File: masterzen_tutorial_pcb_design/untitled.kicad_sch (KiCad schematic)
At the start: 192 parts, among them SW1 SW_Push, SW10 SW_Push, SW11 SW_Push, SW12 SW_Push, SW13 SW_Push, SW14 SW_Push, SW15 SW_Push, SW16 SW_Push, SW17 SW_Push, SW18 SW_Push, SW19 SW_Push, SW2 SW_Push, SW20 SW_Push, SW21 SW_Push, SW22 SW_Push, SW23 SW_Push, SW24 SW_Push, SW25 SW_Push, SW26 SW_Push, SW27 SW_Push, SW28 SW_Push, SW29 SW_Push, SW3 SW_Push, SW30 SW_Push, SW31 SW_Push, SW32 SW_Push, SW33 SW_Push, SW34 SW_Push, SW35 SW_Push, SW36 SW_Push, SW37 SW_Push, SW38 SW_Push, SW39 SW_Push, SW4 SW_Push, SW40 SW_Push, SW41 SW_Push, SW42 SW_Push, SW43 SW_Push, SW44 SW_Push, SW45 SW_Push, SW46 SW_Push, SW47 SW_Push, SW48 SW_Push, SW49 SW_Push, SW5 SW_Push, SW50 SW_Push, SW51 SW_Push, SW52 SW_Push, SW53 SW_Push, SW54 SW_Push, SW55 SW_Push, SW56 SW_Push, SW57 SW_Push, SW58 SW_Push, SW59 SW_Push, SW6 SW_Push, SW60 SW_Push, SW61 SW_Push, SW62 SW_Push, SW63 SW_Push, SW64 SW_Push, SW65 SW_Push, SW66 SW_Push, SW67 SW_Push, SW68 SW_Push, SW69 SW_Push, SW7 SW_Push, SW70 SW_Push, SW71 SW_Push, SW72 SW_Push, SW73 SW_Push, SW74 SW_Push, SW75 SW_Push, SW76 SW_Push, SW77 SW_Push, SW78 SW_Push, SW79 SW_Push, SW8 SW_Push, SW80 SW_Push, SW81 SW_Push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

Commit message: Updated Schematic with correct keys
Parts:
- removed D31, D47, D62, D63, D76, D78, D84, D85, D87, D88, D89, D92: D, symbol Device:D
- removed SW31, SW47, SW62, SW63, SW76, SW78, SW84, SW85, SW87, SW88, SW89, SW92: SW_Push, symbol Switch:SW_Push
- renumbered D32 to D31, D33 to D32, D34 to D33, D35 to D34, D36 to D35, D37 to D36, D38 to D37, D39 to D38, D40 to D39, D41 to D40, D42 to D41, D43 to D42, D44 to D43, D45 to D44, D46 to D45, D48 to D46, D49 to D47, D50 to D48, D51 to D49, D52 to D50, D53 to D51, D54 to D52, D55 to D53, D56 to D54, D57 to D55, D58 to D56, D59 to D57, D60 to D58, D61 to D59, D64 to D60, D65 to D61, D66 to D62, D67 to D63, D68 to D64, D69 to D65, D70 to D66, D71 to D67, D72 to D68, D73 to D69, D74 to D70, D75 to D71, D77 to D72, D79 to D73, D80 to D74, D81 to D75, D82 to D76, D83 to D77, D86 to D78, D90 to D79, D91 to D80, D93 to D81, D94 to D82, D95 to D83, D96 to D84, SW32 to SW31, SW33 to SW32, SW34 to SW33, SW35 to SW34, SW36 to SW35, SW37 to SW36, SW38 to SW37, SW39 to SW38, SW40 to SW39, SW41 to SW40, SW42 to SW41, SW43 to SW42, SW44 to SW43, SW45 to SW44, SW46 to SW45, SW48 to SW46, SW49 to SW47, SW50 to SW48, SW51 to SW49, SW52 to SW50, SW53 to SW51, SW54 to SW52, SW55 to SW53, SW56 to SW54, SW57 to SW55, SW58 to SW56, SW59 to SW57, SW60 to SW58, SW61 to SW59, SW64 to SW60, SW65 to SW61, SW66 to SW62, SW67 to SW63, SW68 to SW64, SW69 to SW65, SW70 to SW66, SW71 to SW67, SW72 to SW68, SW73 to SW69, SW74 to SW70, SW75 to SW71, SW77 to SW72, SW79 to SW73, SW80 to SW74, SW81 to SW75, SW82 to SW76, SW83 to SW77, SW86 to SW78, SW90 to SW79, SW91 to SW80, SW93 to SW81, SW94 to SW82, SW95 to SW83, SW96 to SW84
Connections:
- net col15: now reaches SW16.2, SW31.2, SW46.2, SW60.2, SW74.2, SW84.2
- net col1: now reaches SW18.2, SW2.2, SW33.2, SW48.2, SW62.2, SW76.2
- net col6: now reaches SW23.2, SW38.2, SW53.2, SW67.2, SW7.2
- net col13: now reaches SW14.2, SW30.2, SW45.2, SW82.2
- net col8: now reaches SW25.2, SW40.2, SW55.2, SW69.2, SW9.2
- net row2: now reaches D32.1 (K), D33.1 (K), D34.1 (K), D35.1 (K), D36.1 (K), D37.1 (K), D38.1 (K), D39.1 (K), D40.1 (K), D41.1 (K), D42.1 (K), D43.1 (K), D44.1 (K), D45.1 (K), D46.1 (K)
- net row4: now reaches D61.1 (K), D62.1 (K), D63.1 (K), D64.1 (K), D65.1 (K), D66.1 (K), D67.1 (K), D68.1 (K), D69.1 (K), D70.1 (K), D71.1 (K), D72.1 (K), D73.1 (K), D74.1 (K)
- net col14: now reaches SW15.2, SW73.2, SW83.2
- net row0: now reaches D1.1 (K), D10.1 (K), D11.1 (K), D12.1 (K), D13.1 (K), D14.1 (K), D15.1 (K), D16.1 (K), D2.1 (K), D3.1 (K), D4.1 (K), D5.1 (K), D6.1 (K), D7.1 (K), D8.1 (K), D9.1 (K)
- net row5: now reaches D75.1 (K), D76.1 (K), D77.1 (K), D78.1 (K), D79.1 (K), D80.1 (K), D81.1 (K), D82.1 (K), D83.1 (K), D84.1 (K)
- net row1: now reaches D17.1 (K), D18.1 (K), D19.1 (K), D20.1 (K), D21.1 (K), D22.1 (K), D23.1 (K), D24.1 (K), D25.1 (K), D26.1 (K), D27.1 (K), D28.1 (K), D29.1 (K), D30.1 (K), D31.1 (K)
- net col2: now reaches SW19.2, SW3.2, SW34.2, SW49.2, SW63.2, SW77.2
- net row3: now reaches D47.1 (K), D48.1 (K), D49.1 (K), D50.1 (K), D51.1 (K), D52.1 (K), D53.1 (K), D54.1 (K), D55.1 (K), D56.1 (K), D57.1 (K), D58.1 (K), D59.1 (K), D60.1 (K)
- net col10: now reaches SW11.2, SW27.2, SW42.2, SW57.2, SW71.2, SW80.2
- net col5: now reaches SW22.2, SW37.2, SW52.2, SW6.2, SW66.2, SW78.2
- net col11: now reaches SW12.2, SW28.2, SW43.2, SW58.2
- net col9: now reaches SW10.2, SW26.2, SW41.2, SW56.2, SW70.2, SW79.2
- net col4: now reaches SW21.2, SW36.2, SW5.2, SW51.2, SW65.2
- net col7: now reaches SW24.2, SW39.2, SW54.2, SW68.2, SW8.2
- net col0: now reaches SW1.2, SW17.2, SW32.2, SW47.2, SW61.2, SW75.2
- net col3: now reaches SW20.2, SW35.2, SW4.2, SW50.2, SW64.2
- net col12: now reaches SW13.2, SW29.2, SW44.2, SW59.2, SW72.2, SW81.2

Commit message: finished schematic
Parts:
- removed D15, D16, D45, D64, D67, D75, D76, D77, D78, D79, D80, D81, D82, D83, D84: D, symbol Device:D
- removed SW15, SW16, SW45, SW64, SW65, SW68, SW75, SW76, SW77, SW78, SW79, SW80, SW81, SW82, SW83, SW84: SW_Push, symbol Switch:SW_Push
- added D17, D46, D66: D, Diode_SMD:D_SOD-123, symbol Device:D
- added SW17: left arrow, Alps_Only:ALPS-1U, symbol Switch:SW_Push
- added SW18: end, Alps_Only:ALPS-1U, symbol Switch:SW_Push
- added SW47: Pause ScrLk, Alps_Only:ALPS-1U, symbol Switch:SW_Push
- added SW66: PrtSc NmLk, Alps_Only:ALPS-1U, symbol Switch:SW_Push
- D10: renamed from D9; footprint (none) -> Diode_SMD:D_SOD-123
- D11: renamed from D10; footprint (none) -> Diode_SMD:D_SOD-123
- D12: renamed from D11; footprint (none) -> Diode_SMD:D_SOD-123
- D13: renamed from D12; footprint (none) -> Diode_SMD:D_SOD-123
- D14: renamed from D13; footprint (none) -> Diode_SMD:D_SOD-123
- D15: renamed from D14; footprint (none) -> Diode_SMD:D_SOD-123
- D18: renamed from D17; footprint (none) -> Diode_SMD:D_SOD-123
- D19: renamed from D18; footprint (none) -> Diode_SMD:D_SOD-123
- D2: renamed from D1; footprint (none) -> Diode_SMD:D_SOD-123
- D20: renamed from D19; footprint (none) -> Diode_SMD:D_SOD-123
- D21: renamed from D20; footprint (none) -> Diode_SMD:D_SOD-123
- D22: renamed from D21; footprint (none) -> Diode_SMD:D_SOD-123
- D23: renamed from D22; footprint (none) -> Diode_SMD:D_SOD-123
- D24: renamed from D23; footprint (none) -> Diode_SMD:D_SOD-123
- D25: renamed from D24; footprint (none) -> Diode_SMD:D_SOD-123
- D26: renamed from D25; footprint (none) -> Diode_SMD:D_SOD-123
- D27: renamed from D26; footprint (none) -> Diode_SMD:D_SOD-123
- D28: renamed from D27; footprint (none) -> Diode_SMD:D_SOD-123
- D29: renamed from D28; footprint (none) -> Diode_SMD:D_SOD-123
- D3: renamed from D2; footprint (none) -> Diode_SMD:D_SOD-123
- D30: renamed from D29; footprint (none) -> Diode_SMD:D_SOD-123
- D31: renamed from D30; footprint (none) -> Diode_SMD:D_SOD-123
- D32: renamed from D31; footprint (none) -> Diode_SMD:D_SOD-123
- D33: renamed from D32; footprint (none) -> Diode_SMD:D_SOD-123
- D34: renamed from D33; footprint (none) -> Diode_SMD:D_SOD-123
- D35: renamed from D34; footprint (none) -> Diode_SMD:D_SOD-123
- D36: renamed from D35; footprint (none) -> Diode_SMD:D_SOD-123
- D37: renamed from D36; footprint (none) -> Diode_SMD:D_SOD-123
- D38: renamed from D37; footprint (none) -> Diode_SMD:D_SOD-123
- D39: renamed from D38; footprint (none) -> Diode_SMD:D_SOD-123
- D4: renamed from D3; footprint (none) -> Diode_SMD:D_SOD-123
- D40: renamed from D39; footprint (none) -> Diode_SMD:D_SOD-123
- D41: renamed from D40; footprint (none) -> Diode_SMD:D_SOD-123
- D42: renamed from D41; footprint (none) -> Diode_SMD:D_SOD-123
- D43: renamed from D42; footprint (none) -> Diode_SMD:D_SOD-123
- D44: renamed from D43; footprint (none) -> Diode_SMD:D_SOD-123
- D45: renamed from D44; footprint (none) -> Diode_SMD:D_SOD-123
- D47: renamed from D46; footprint (none) -> Diode_SMD:D_SOD-123
- D48: renamed from D47; footprint (none) -> Diode_SMD:D_SOD-123
- D49: renamed from D48; footprint (none) -> Diode_SMD:D_SOD-123
- D5: renamed from D4; footprint (none) -> Diode_SMD:D_SOD-123
- D50: renamed from D49; footprint (none) -> Diode_SMD:D_SOD-123
- D51: renamed from D50; footprint (none) -> Diode_SMD:D_SOD-123
- D52: renamed from D51; footprint (none) -> Diode_SMD:D_SOD-123
- D53: renamed from D52; footprint (none) -> Diode_SMD:D_SOD-123
- D54: renamed from D53; footprint (none) -> Diode_SMD:D_SOD-123
- D55: renamed from D54; footprint (none) -> Diode_SMD:D_SOD-123
- D56: renamed from D55; footprint (none) -> Diode_SMD:D_SOD-123
- D57: renamed from D56; footprint (none) -> Diode_SMD:D_SOD-123
- D58: renamed from D57; footprint (none) -> Diode_SMD:D_SOD-123
- D59: renamed from D58; footprint (none) -> Diode_SMD:D_SOD-123
- D6: renamed from D5; footprint (none) -> Diode_SMD:D_SOD-123
- D60: renamed from D59; footprint (none) -> Diode_SMD:D_SOD-123
- D61: renamed from D60; footprint (none) -> Diode_SMD:D_SOD-123
- D62: renamed from D61; footprint (none) -> Diode_SMD:D_SOD-123
- D63: renamed from D62; footprint (none) -> Diode_SMD:D_SOD-123
- D64: renamed from D63; footprint (none) -> Diode_SMD:D_SOD-123
- D65, D68: footprint (none) -> Diode_SMD:D_SOD-123
- D67: renamed from D66; footprint (none) -> Diode_SMD:D_SOD-123
- D7: renamed from D6; footprint (none) -> Diode_SMD:D_SOD-123
- D70: renamed from D69; footprint (none) -> Diode_SMD:D_SOD-123
- D71: renamed from D70; footprint (none) -> Diode_SMD:D_SOD-123
- D72: renamed from D71; footprint (none) -> Diode_SMD:D_SOD-123
- D73: renamed from D72; footprint (none) -> Diode_SMD:D_SOD-123
- D74: renamed from D73; footprint (none) -> Diode_SMD:D_SOD-123
- D75: renamed from D74; footprint (none) -> Diode_SMD:D_SOD-123
- D8: renamed from D7; footprint (none) -> Diode_SMD:D_SOD-123
- D9: renamed from D8; footprint (none) -> Diode_SMD:D_SOD-123
- SW10: renamed from SW8; value SW_Push -> & 7; footprint (none) -> Alps_Only:ALPS-1U
- SW11: renamed from SW9; value SW_Push -> * 8; footprint (none) -> Alps_Only:ALPS-1U
- SW12: renamed from SW10; value SW_Push -> ( 9; footprint (none) -> Alps_Only:ALPS-1U
- SW13: renamed from SW11; value SW_Push -> ) 0; footprint (none) -> Alps_Only:ALPS-1U
- SW14: renamed from SW12; value SW_Push -> _ -; footprint (none) -> Alps_Only:ALPS-1U
- SW15: renamed from SW13; value SW_Push -> + =; footprint (none) -> Alps_Only:ALPS-1U
- SW16: renamed from SW14; value SW_Push -> Delete/Insert; footprint (none) -> Alps_Only:ALPS-1U
- SW19: renamed from SW17; value SW_Push -> Tab; footprint (none) -> Alps_Only:ALPS-1U
- SW20: renamed from SW18; value SW_Push -> Q; footprint (none) -> Alps_Only:ALPS-1U
- SW21: renamed from SW19; value SW_Push -> W; footprint (none) -> Alps_Only:ALPS-1U
- SW22: renamed from SW20; value SW_Push -> E; footprint (none) -> Alps_Only:ALPS-1U
- SW23: renamed from SW21; value SW_Push -> R; footprint (none) -> Alps_Only:ALPS-1U
- SW24: renamed from SW22; value SW_Push -> T; footprint (none) -> Alps_Only:ALPS-1U
- SW25: renamed from SW23; value SW_Push -> Y; footprint (none) -> Alps_Only:ALPS-1U
- SW26: renamed from SW24; value SW_Push -> U; footprint (none) -> Alps_Only:ALPS-1U
- SW27: renamed from SW25; value SW_Push -> I; footprint (none) -> Alps_Only:ALPS-1U
- SW28: renamed from SW26; value SW_Push -> O; footprint (none) -> Alps_Only:ALPS-1U
- SW29: renamed from SW27; value SW_Push -> P; footprint (none) -> Alps_Only:ALPS-1U
- SW3: renamed from SW1; value SW_Push -> ESC; footprint (none) -> Alps_Only:ALPS-1U
- SW30: renamed from SW28; value SW_Push -> [; footprint (none) -> Alps_Only:ALPS-1U
- SW31: renamed from SW29; value SW_Push -> ]; footprint (none) -> Alps_Only:ALPS-1U
- SW32: renamed from SW30; value SW_Push -> Backspace; footprint (none) -> Alps_Only:ALPS-1U
- SW33: renamed from SW31; value SW_Push -> Home; footprint (none) -> Alps_Only:ALPS-1U
- SW34: renamed from SW32; value SW_Push -> Caps Lock; footprint (none) -> Alps_Only:ALPS-1U
- SW35: renamed from SW33; value SW_Push -> A; footprint (none) -> Alps_Only:ALPS-1U
- SW36: renamed from SW34; value SW_Push -> S; footprint (none) -> Alps_Only:ALPS-1U
- SW37: renamed from SW35; value SW_Push -> D; footprint (none) -> Alps_Only:ALPS-1U
- SW38: renamed from SW36; value SW_Push -> F; footprint (none) -> Alps_Only:ALPS-1U
- SW39: renamed from SW37; value SW_Push -> G; footprint (none) -> Alps_Only:ALPS-1U
- SW4: renamed from SW2; value SW_Push -> ! 1; footprint (none) -> Alps_Only:ALPS-1U
- SW40: renamed from SW38; value SW_Push -> H; footprint (none) -> Alps_Only:ALPS-1U
- SW41: renamed from SW39; value SW_Push -> J; footprint (none) -> Alps_Only:ALPS-1U
- SW42: renamed from SW40; value SW_Push -> K; footprint (none) -> Alps_Only:ALPS-1U
- SW43: renamed from SW41; value SW_Push -> L; footprint (none) -> Alps_Only:ALPS-1U
- SW44: renamed from SW42; value SW_Push -> :; footprint (none) -> Alps_Only:ALPS-1U
- SW45: renamed from SW43; value SW_Push -> :; footprint (none) -> Alps_Only:ALPS-1U
- SW46: renamed from SW44; value SW_Push -> Enter; footprint (none) -> Alps_Only:ALPS-1U
- SW48: renamed from SW46; value SW_Push -> Page Up; footprint (none) -> Alps_Only:ALPS-1U
- SW49: renamed from SW47; value SW_Push -> left Shift; footprint (none) -> Alps_Only:ALPS-1U
- SW5: renamed from SW3; value SW_Push -> @ 2; footprint (none) -> Alps_Only:ALPS-1U
- SW50: renamed from SW48; value SW_Push -> Z; footprint (none) -> Alps_Only:ALPS-1U
- SW51: renamed from SW49; value SW_Push -> X; footprint (none) -> Alps_Only:ALPS-1U
- SW52: renamed from SW50; value SW_Push -> C; footprint (none) -> Alps_Only:ALPS-1U
- SW53: renamed from SW51; value SW_Push -> V; footprint (none) -> Alps_Only:ALPS-1U
- SW54: renamed from SW52; value SW_Push -> B; footprint (none) -> Alps_Only:ALPS-1U
- SW55: renamed from SW53; value SW_Push -> N; footprint (none) -> Alps_Only:ALPS-1U
- SW56: renamed from SW54; value SW_Push -> M; footprint (none) -> Alps_Only:ALPS-1U
- SW57: renamed from SW55; value SW_Push -> ,; footprint (none) -> Alps_Only:ALPS-1U
- SW58: renamed from SW56; value SW_Push -> .; footprint (none) -> Alps_Only:ALPS-1U
- SW59: renamed from SW57; value SW_Push -> /; footprint (none) -> Alps_Only:ALPS-1U
- SW6: renamed from SW4; value SW_Push -> # 3; footprint (none) -> Alps_Only:ALPS-1U
- SW60: renamed from SW58; value SW_Push -> right shift; footprint (none) -> Alps_Only:ALPS-1U
- SW61: renamed from SW59; value SW_Push -> up arrow; footprint (none) -> Alps_Only:ALPS-1U
- SW62: renamed from SW60; value SW_Push -> Page Down; footprint (none) -> Alps_Only:ALPS-1U
- SW63: renamed from SW61; value SW_Push -> Ctrl; footprint (none) -> Alps_Only:ALPS-1U
- SW64: renamed from SW62; value SW_Push -> Win; footprint (none) -> Alps_Only:ALPS-1U
- SW65: renamed from SW63; value SW_Push -> Alt; footprint (none) -> Alps_Only:ALPS-1U
- SW67: value SW_Push -> Delete Insert; footprint (none) -> Alps_Only:ALPS-1U
- SW68: renamed from SW66; value SW_Push -> Space bar; footprint (none) -> Alps_Only:ALPS-1U
- SW7: renamed from SW5; value SW_Push -> $ 4; footprint (none) -> Alps_Only:ALPS-1U
- SW71: renamed from SW69; value SW_Push -> Alt; footprint (none) -> Alps_Only:ALPS-1U
- SW72: renamed from SW70; value SW_Push -> Fn; footprint (none) -> Alps_Only:ALPS-1U
- SW73: renamed from SW71; value SW_Push -> right Ctrl; footprint (none) -> Alps_Only:ALPS-1U
- SW74: renamed from SW72; value SW_Push -> down arrow; footprint (none) -> Alps_Only:ALPS-1U
- SW75: renamed from SW73; value SW_Push -> right arrow; footprint (none) -> Alps_Only:ALPS-1U
- SW76: renamed from SW74; value SW_Push -> End; footprint (none) -> Alps_Only:ALPS-1U
- SW8: renamed from SW6; value SW_Push -> % 5; footprint (none) -> Alps_Only:ALPS-1U
- SW9: renamed from SW7; value SW_Push -> ^ 6; footprint (none) -> Alps_Only:ALPS-1U
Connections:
- net col11: now also SW17.2
- net col14: now also SW67.2, SW47.2, SW66.2
- net col6: no longer SW67.2
- net row1: now also D68.1 (K)
- net row2: now also D66.1 (K)
- net row3: now also D65.1 (K)
- net row4: now also D17.1 (K); no longer D65.1 (K), D68.1 (K)
- net at SW67.1: now also D68.2 (A)
- net at D65.2 (A): now also SW47.1
- net col15 renamed ROT_ENC_COL
- net ROT_ENC_COL: now also SW18.2
- net row0 renamed ROT_ENC_ROW
- net ROT_ENC_ROW: now also D46.1 (K)
- new net: D17.2 (A), SW17.1
- new net: D66.2 (A), SW66.1
- new net: D46.2 (A), SW18.1

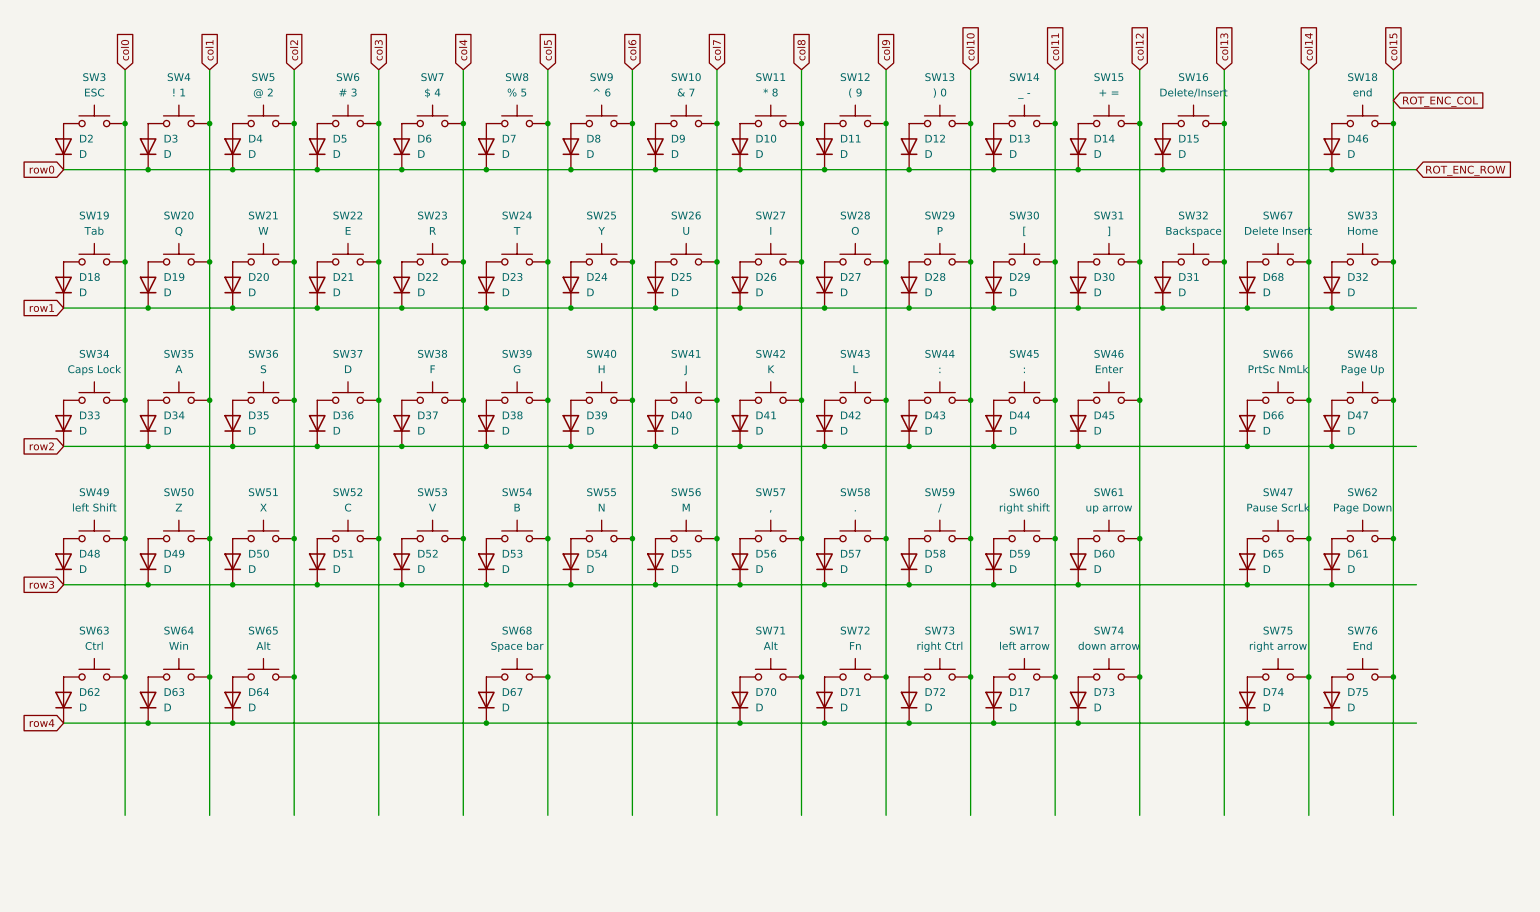
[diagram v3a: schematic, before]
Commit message: starting placing components on a pcb
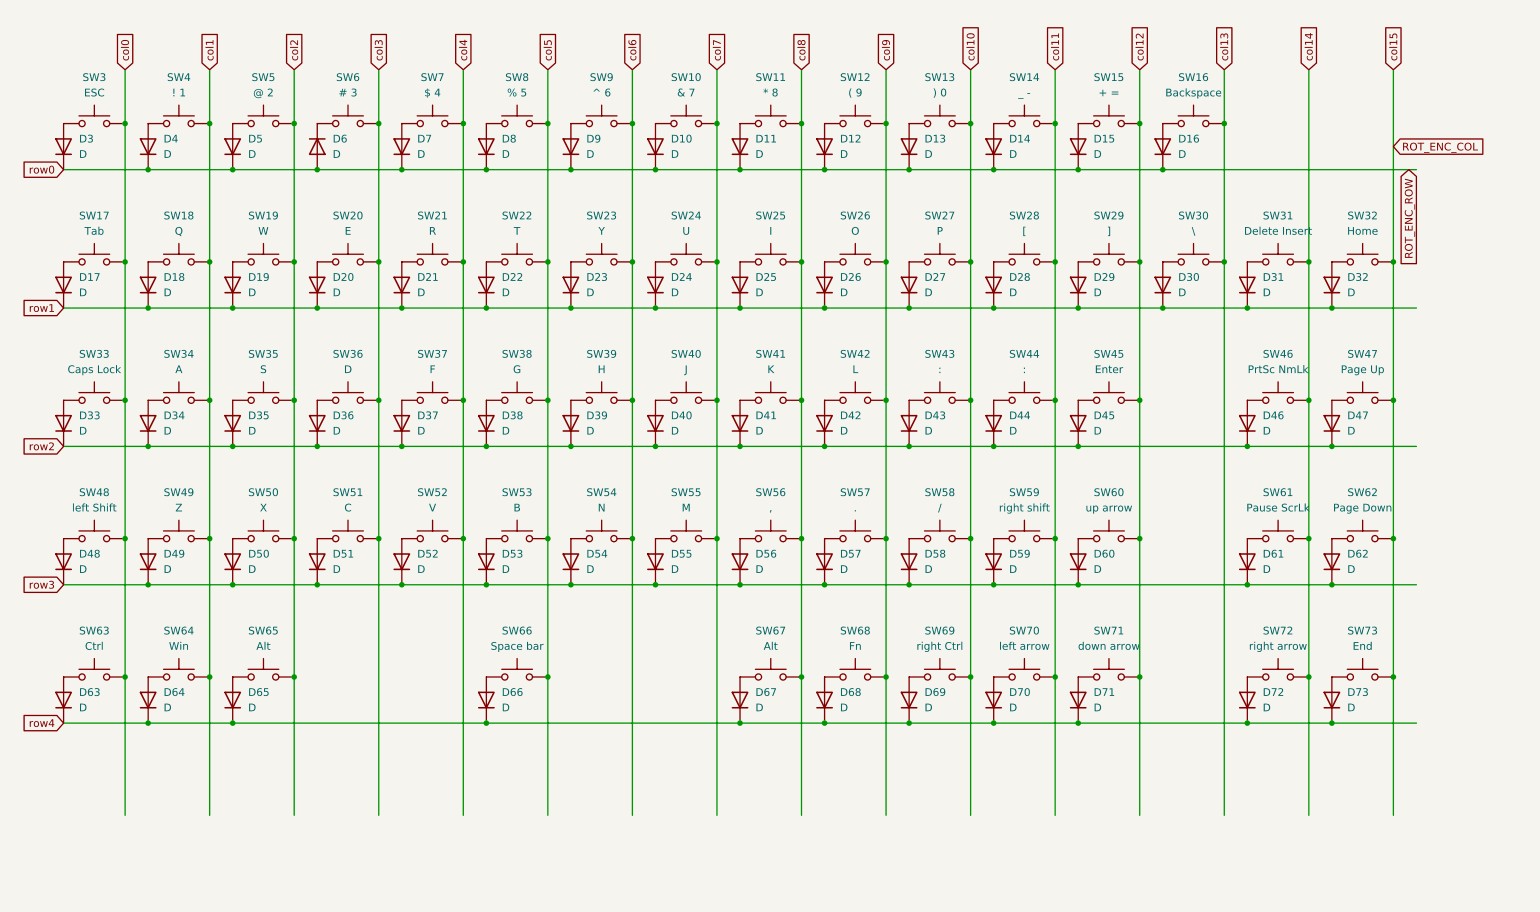
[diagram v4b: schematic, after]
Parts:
- removed D46: D, Diode_SMD:D_SOD-123, symbol Device:D
- removed SW18: end, Alps_Only:ALPS-1U, symbol Switch:SW_Push
- SW10, SW11, SW12, SW13, SW14, SW15, SW3, SW4, SW5, SW6, SW62, SW7, SW8, SW9: footprint Alps_Only:ALPS-1U -> MX_Only:MXOnly-1U-NoLED
- SW16: value Delete/Insert -> Backspace; footprint Alps_Only:ALPS-1U -> MX_Only:MXOnly-2U-NoLED
- SW17: renamed from SW19; footprint Alps_Only:ALPS-1U -> MX_Only:MXOnly-1.5U-NoLED
- SW18: renamed from SW20; footprint Alps_Only:ALPS-1U -> MX_Only:MXOnly-1U-NoLED
- SW19: renamed from SW21; footprint Alps_Only:ALPS-1U -> MX_Only:MXOnly-1U-NoLED
- SW20: renamed from SW22; footprint Alps_Only:ALPS-1U -> MX_Only:MXOnly-1U-NoLED
- SW21: renamed from SW23; footprint Alps_Only:ALPS-1U -> MX_Only:MXOnly-1U-NoLED
- SW22: renamed from SW24; footprint Alps_Only:ALPS-1U -> MX_Only:MXOnly-1U-NoLED
- SW23: renamed from SW25; footprint Alps_Only:ALPS-1U -> MX_Only:MXOnly-1U-NoLED
- SW24: renamed from SW26; footprint Alps_Only:ALPS-1U -> MX_Only:MXOnly-1U-NoLED
- SW25: renamed from SW27; footprint Alps_Only:ALPS-1U -> MX_Only:MXOnly-1U-NoLED
- SW26: renamed from SW28; footprint Alps_Only:ALPS-1U -> MX_Only:MXOnly-1U-NoLED
- SW27: renamed from SW29; footprint Alps_Only:ALPS-1U -> MX_Only:MXOnly-1U-NoLED
- SW28: renamed from SW30; footprint Alps_Only:ALPS-1U -> MX_Only:MXOnly-1U-NoLED
- SW29: renamed from SW31; footprint Alps_Only:ALPS-1U -> MX_Only:MXOnly-1U-NoLED
- SW30: renamed from SW32; value Backspace -> \; footprint Alps_Only:ALPS-1U -> MX_Only:MXOnly-1.5U-NoLED
- SW31: renamed from SW67; footprint Alps_Only:ALPS-1U -> MX_Only:MXOnly-1U-NoLED
- SW32: renamed from SW33; footprint Alps_Only:ALPS-1U -> MX_Only:MXOnly-1U-NoLED
- SW33: renamed from SW34; footprint Alps_Only:ALPS-1U -> MX_Only:MXOnly-1.75U-NoLED
- SW34: renamed from SW35; footprint Alps_Only:ALPS-1U -> MX_Only:MXOnly-1U-NoLED
- SW35: renamed from SW36; footprint Alps_Only:ALPS-1U -> MX_Only:MXOnly-1U-NoLED
- SW36: renamed from SW37; footprint Alps_Only:ALPS-1U -> MX_Only:MXOnly-1U-NoLED
- SW37: renamed from SW38; footprint Alps_Only:ALPS-1U -> MX_Only:MXOnly-1U-NoLED
- SW38: renamed from SW39; footprint Alps_Only:ALPS-1U -> MX_Only:MXOnly-1U-NoLED
- SW39: renamed from SW40; footprint Alps_Only:ALPS-1U -> MX_Only:MXOnly-1U-NoLED
- SW40: renamed from SW41; footprint Alps_Only:ALPS-1U -> MX_Only:MXOnly-1U-NoLED
- SW41: renamed from SW42; footprint Alps_Only:ALPS-1U -> MX_Only:MXOnly-1U-NoLED
- SW42: renamed from SW43; footprint Alps_Only:ALPS-1U -> MX_Only:MXOnly-1U-NoLED
- SW43: renamed from SW44; footprint Alps_Only:ALPS-1U -> MX_Only:MXOnly-1U-NoLED
- SW44: renamed from SW45; footprint Alps_Only:ALPS-1U -> MX_Only:MXOnly-1U-NoLED
- SW45: renamed from SW46; footprint Alps_Only:ALPS-1U -> MX_Only:MXOnly-2.25U-NoLED
- SW46: renamed from SW66; footprint Alps_Only:ALPS-1U -> MX_Only:MXOnly-1U-NoLED
- SW47: renamed from SW48; footprint Alps_Only:ALPS-1U -> MX_Only:MXOnly-1U-NoLED
- SW48: renamed from SW49; footprint Alps_Only:ALPS-1U -> MX_Only:MXOnly-2.25U-NoLED
- SW49: renamed from SW50; footprint Alps_Only:ALPS-1U -> MX_Only:MXOnly-1U-NoLED
- SW50: renamed from SW51; footprint Alps_Only:ALPS-1U -> MX_Only:MXOnly-1U-NoLED
- SW51: renamed from SW52; footprint Alps_Only:ALPS-1U -> MX_Only:MXOnly-1U-NoLED
- SW52: renamed from SW53; footprint Alps_Only:ALPS-1U -> MX_Only:MXOnly-1U-NoLED
- SW53: renamed from SW54; footprint Alps_Only:ALPS-1U -> MX_Only:MXOnly-1U-NoLED
- SW54: renamed from SW55; footprint Alps_Only:ALPS-1U -> MX_Only:MXOnly-1U-NoLED
- SW55: renamed from SW56; footprint Alps_Only:ALPS-1U -> MX_Only:MXOnly-1U-NoLED
- SW56: renamed from SW57; footprint Alps_Only:ALPS-1U -> MX_Only:MXOnly-1U-NoLED
- SW57: renamed from SW58; footprint Alps_Only:ALPS-1U -> MX_Only:MXOnly-1U-NoLED
- SW58: renamed from SW59; footprint Alps_Only:ALPS-1U -> MX_Only:MXOnly-1U-NoLED
- SW59: renamed from SW60; footprint Alps_Only:ALPS-1U -> MX_Only:MXOnly-1.75U-NoLED
- SW60: renamed from SW61; footprint Alps_Only:ALPS-1U -> MX_Only:MXOnly-1U-NoLED
- SW61: renamed from SW47; footprint Alps_Only:ALPS-1U -> MX_Only:MXOnly-1U-NoLED
- SW63, SW64, SW65: footprint Alps_Only:ALPS-1U -> MX_Only:MXOnly-1.25U-NoLED
- SW66: renamed from SW68; footprint Alps_Only:ALPS-1U -> MX_Only:MXOnly-6.25U-NoLED
- SW67: renamed from SW71; footprint Alps_Only:ALPS-1U -> MX_Only:MXOnly-1U-NoLED
- SW68: renamed from SW72; footprint Alps_Only:ALPS-1U -> MX_Only:MXOnly-1U-NoLED
- SW69: renamed from SW73; footprint Alps_Only:ALPS-1U -> MX_Only:MXOnly-1U-NoLED
- SW70: renamed from SW17; footprint Alps_Only:ALPS-1U -> MX_Only:MXOnly-1U-NoLED
- SW71: renamed from SW74; footprint Alps_Only:ALPS-1U -> MX_Only:MXOnly-1U-NoLED
- SW72: renamed from SW75; footprint Alps_Only:ALPS-1U -> MX_Only:MXOnly-1U-NoLED
- SW73: renamed from SW76; footprint Alps_Only:ALPS-1U -> MX_Only:MXOnly-1U-NoLED
- renumbered D9 to D10, D10 to D11, D11 to D12, D12 to D13, D13 to D14, D14 to D15, D15 to D16, D18 to D17, D19 to D18, D20 to D19, D21 to D20, D22 to D21, D23 to D22, D24 to D23, D25 to D24, D26 to D25, D27 to D26, D28 to D27, D29 to D28, D30 to D29, D2 to D3, D31 to D30, D68 to D31, D3 to D4, D66 to D46, D4 to D5, D5 to D6, D65 to D61, D61 to D62, D62 to D63, D63 to D64, D64 to D65, D67 to D66, D70 to D67, D71 to D68, D72 to D69, D6 to D7, D17 to D70, D73 to D71, D74 to D72, D75 to D73, D7 to D8, D8 to D9
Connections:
- net ROT_ENC_ROW: now also D6.2 (A); no longer D6.1 (K)
- net at SW6.1: now also D6.1 (K); no longer D6.2 (A)
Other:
- moved on the sheet: D6

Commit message: routed matrix
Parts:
- added D17: D, Diode_SMD:D_SOD-123, symbol Device:D
- renumbered D17 to D18, D18 to D19, D19 to D20, D20 to D21, D21 to D22, D22 to D23, D23 to D24, D24 to D25, D25 to D26, D26 to D27, D27 to D28, D28 to D29, D29 to D30, D30 to D31, D31 to D32, D32 to D33, D33 to D34, D34 to D35, D35 to D36, D36 to D37, D37 to D38, D38 to D39, D39 to D40, D40 to D41, D41 to D42, D42 to D43, D43 to D44, D44 to D45, D45 to D46, D46 to D47, D47 to D48, D48 to D49, D49 to D50, D50 to D51, D51 to D52, D52 to D53, D53 to D54, D54 to D55, D55 to D56, D56 to D57, D57 to D58, D58 to D59, D59 to D60, D60 to D61, D61 to D62, D62 to D63, D63 to D64, D64 to D65, D65 to D66, D66 to D67, D67 to D68, D68 to D69, D69 to D70, D70 to D71, D71 to D72, D72 to D73, D73 to D74
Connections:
- net ROT_ENC_ROW: now also D17.2 (A); no longer D10.1 (K), D11.1 (K), D12.1 (K), D13.1 (K), D14.1 (K), D15.1 (K), D16.1 (K), D3.1 (K), D4.1 (K), D5.1 (K), D6.2 (A), D7.1 (K), D8.1 (K), D9.1 (K)
- new net row0: D10.1 (K), D11.1 (K), D12.1 (K), D13.1 (K), D14.1 (K), D15.1 (K), D16.1 (K), D17.1 (K), D3.1 (K), D4.1 (K), D5.1 (K), D6.2 (A), D7.1 (K), D8.1 (K), D9.1 (K)
